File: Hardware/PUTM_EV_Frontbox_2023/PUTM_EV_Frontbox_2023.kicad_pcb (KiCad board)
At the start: 4 copper layers, 97 x 70 mm, 236 parts, among them J1 Conn_02x15_Counter_Clockwise, J3 STLINK-V3MINIE, K2 FINDER-32.21-x000, Q1 NX7002AK, SW1 Reset switch, U1 STM32G473RCTx, U10 TLP291-4, U11 TLP291-4, U12 MCP2542FDxMF, U13 MCP6001, U14 MCP6N11-005, U15 MCP6001, U16 MCP6N11-005, U17 MCP6002-xMC, U18 MCP6N11-005, U19 TLV743P, U2 MCP6002-xMC, U20 LM4040DBZ-5, U21 MCP6001, U22 MCP6N11-005, U23 MCP6001, U24 MCP6001, U25 MCP6N11-005, U26 MCP6001, U3 IMS330DHCX, U4 TLV743P, U5 TLV743P, U6 BD50FC0FP, U7 LM62440-Q1, U8 MCP2542FDxMF, U9 MCP6N11-005, Y1 ABM8G-48.000MHZ

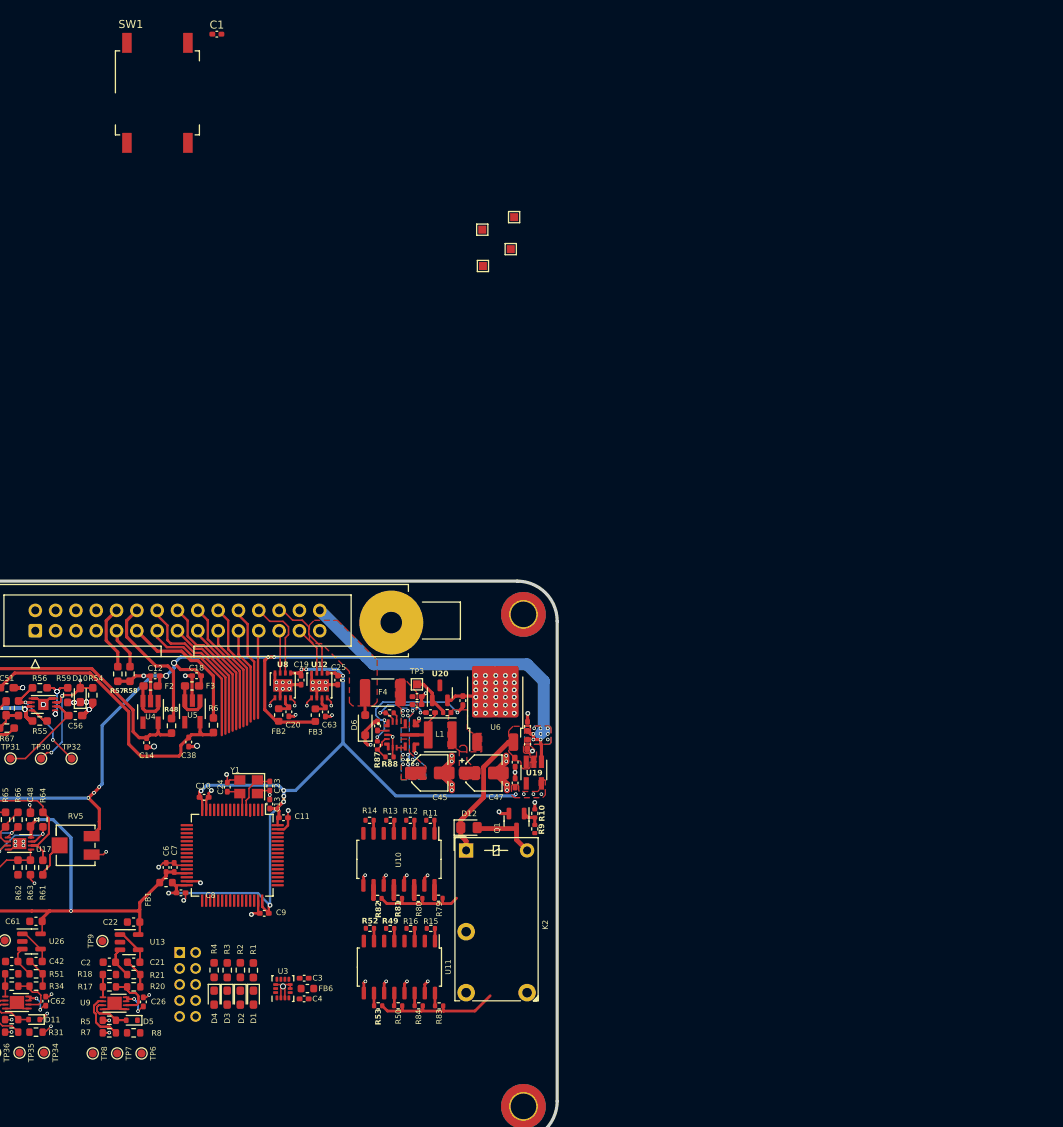
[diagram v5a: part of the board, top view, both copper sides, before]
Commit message: Changed mcu pinout
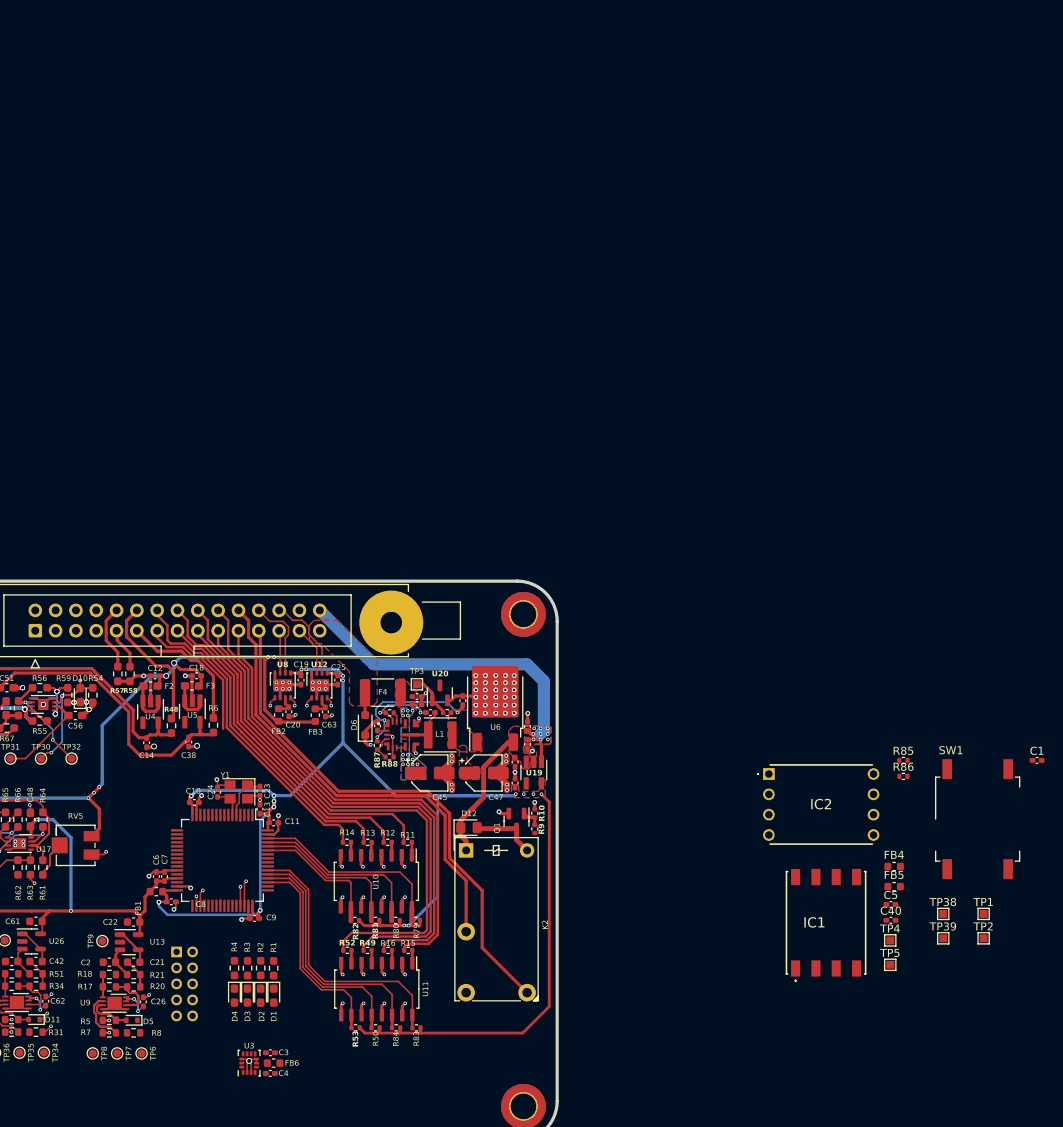
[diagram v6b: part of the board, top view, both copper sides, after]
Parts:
- added C40: 100nF, Capacitor_SMD:C_0402_1005Metric_Pad0.74x0.62mm_HandSolder, F.Cu at (243.7, 60.4)
- added C5: 100nF, Capacitor_SMD:C_0402_1005Metric_Pad0.74x0.62mm_HandSolder, F.Cu at (243.7, 58.4)
- added FB4: 60R@100MHz, Inductor_SMD:L_0603_1608Metric, F.Cu at (244.1, 53.6)
- added FB5: 60R@100MHz, Inductor_SMD:L_0603_1608Metric, F.Cu at (244.1, 56.2)
- added IC1: ELVH-MF12D-HRRJ-C-N3A4, Frontbox:ELVH005DHRRJINAA4, F.Cu at (235.6, 60.7)
- added IC2: ELVH-MF12D-HRRJ-C-N3A4, Frontbox:ELVHL10DHRRDCN2A4, F.Cu at (228.4, 42.1)
- added R85: 4k7, Resistor_SMD:R_0402_1005Metric, F.Cu at (245.2, 40.4)
- added R86: 4k7, Resistor_SMD:R_0402_1005Metric, F.Cu at (245.2, 42.4)
- added TP4: TestPoint, TestPoint:TestPoint_Pad_1.0x1.0mm, F.Cu at (243.6, 62.9)
- added TP5: TestPoint, TestPoint:TestPoint_Pad_1.0x1.0mm, F.Cu at (243.6, 65.9)
- moved SW1 136.9 mm to (254.5, 47.7)
- moved C1 136.9 mm to (262.0, 40.4)
- moved TP39 105.7 mm to (250.2, 62.6), turned to 0 degrees
- moved TP1 105.0 mm to (255.3, 59.6), turned to 0 degrees
- moved TP2 104.5 mm to (255.3, 62.6), turned to 0 degrees
- moved TP38 99.3 mm to (250.2, 59.6), turned to 0 degrees
- moved FB6 10.2 mm to (166.5, 78.2)
- moved C3 10.2 mm to (166.1, 76.9)
- moved C4 10.2 mm to (166.1, 79.5)
- moved U3 10.2 mm to (163.5, 78.2)
- moved R11 3.94 mm to (183.3, 50.6)
- moved R12 3.94 mm to (180.8, 50.6)
- moved R13 3.94 mm to (178.3, 50.6)
- moved R14 3.94 mm to (175.7, 50.6)
- moved R80 3.94 mm to (181.8, 60.4)
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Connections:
- R11 pad 1: /KILL_LEWY -> /BSPD_SENSE
- R13 pad 1: /KILL_KIERA -> /OVERTRAVEL
- R14 pad 1: /INERTIA -> /RIGHT_WHEEL_SC
- R15 pad 1: /BSPD_SENSE -> /KILL_KIERA
- R16 pad 1: /OVERTRAVEL -> /KILL_LEWY
- R52 pad 1: /Safety sense/Safety_Left_Wheel -> /INERTIA
- R53 pad 2: /Safety sense/Sens_Left_Wheel -> /Sense_inertia
- R79 pad 2: /Sense_left -> /Sense_BSPD
- R81 pad 2: /Sense_driver -> /Sense_overtravel
- R82 pad 2: /Sense_inertia -> /Sense_Right_Wheel
- R83 pad 2: /Sense_BSPD -> /Sense_driver
- R84 pad 2: /Sense_overtravel -> /Sense_left
- U1 pad 12: /Safety_control -> unconnected-(U1-PA0-Pad12)
- U1 pad 17: /APPS_sig2 -> /APPS_sig1
- U1 pad 18: /APPS_sig1 -> /APPS_sig2
- U1 pad 21: /SUSP_R_OUT -> /SUSP_L_OUT
- U1 pad 22: /SUSP_L_OUT -> /BRAKE_PRESSURE_FRONT_OUT
- U1 pad 23: /BRAKE_PRESSURE_REAR_OUT -> /SUSP_R_OUT
- U1 pad 24: /BRAKE_PRESSURE_FRONT_OUT -> /BRAKE_PRESSURE_REAR_OUT
- U1 pad 34: /CAN1_RX -> /CAN2_RX
- U1 pad 35: /CAN1_TX -> /CAN2_TX
- U1 pad 36: /DEBUG_LED4 -> unconnected-(U1-PB14-Pad36)
- U1 pad 37: /DEBUG_LED3 -> unconnected-(U1-PB15-Pad37)
- U1 pad 38: /DEBUG_LED2 -> unconnected-(U1-PC6-Pad38)
- U1 pad 39: /DEBUG_LED1 -> unconnected-(U1-PC7-Pad39)
- U1 pad 40: /YAWPROBE_I^{2}C_SCL -> unconnected-(U1-PC8-Pad40)
- U1 pad 41: /YAWPROBE_I^{2}C_SDA -> unconnected-(U1-PC9-Pad41)
- U1 pad 45: unconnected-(U1-PA11-Pad45) -> /CAN1_RX
- U1 pad 46: unconnected-(U1-PA12-Pad46) -> /CAN1_TX
- U1 pad 51: unconnected-(U1-PA15-Pad51) -> /Sense_inertia
- U1 pad 52: unconnected-(U1-PC10-Pad52) -> /Sense_EBS
- U1 pad 53: /Sense_driver -> /Sense_left
- U1 pad 54: /Sense_right -> /Sense_driver
- U1 pad 55: /Sense_inertia -> unconnected-(U1-PD2-Pad55)
- U1 pad 59: /Sense_left -> /Sense_Right_Wheel
- U1 pad 60: /Sense_EBS -> /Sense_overtravel
- U1 pad 61: /Sense_overtravel -> /Sense_right
- U10 pad 10: /Sense_inertia -> /Sense_Right_Wheel
- U10 pad 12: /Sense_driver -> /Sense_overtravel
- U10 pad 16: /Sense_left -> /Sense_BSPD
- U11 pad 10: /Safety sense/Sens_Left_Wheel -> /Sense_inertia
- U11 pad 14: /Sense_overtravel -> /Sense_left
- U11 pad 16: /Sense_BSPD -> /Sense_driver
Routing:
- net +3.3V: track 136.1 -> 192.0 mm, vias 14 -> 16
- net /SAFE-IN: track 11.0 -> 65.8 mm
- net /INERTIA: track 16.8 -> 70.3 mm
- net /EBS_SAFETY: track 13.2 -> 64.6 mm
- net /KILL_LEWY: track 15.8 -> 65.4 mm
- net /KILL_KIERA: track 12.0 -> 59.9 mm
- net /SAFE-OUT: track 14.4 -> 59.0 mm
- net /CAN2_RX: track 1.18 -> 37.0 mm, vias 1 -> 2
- net /CAN2_TX: track 1.21 -> 35.2 mm, vias 1 -> 2
- net /Sense_driver: track 1.62 -> 34.1 mm
- net /Sense_left: track 1.60 -> 31.4 mm
- net /CAN1_RX: track 1.19 -> 29.4 mm, vias 1 -> 2
- net /CAN1_TX: track 1.21 -> 29.3 mm, vias 1 -> 2
- net /BSPD_SENSE: track 14.3 -> 41.7 mm
- net /Sense_EBS: track 1.60 -> 28.6 mm
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
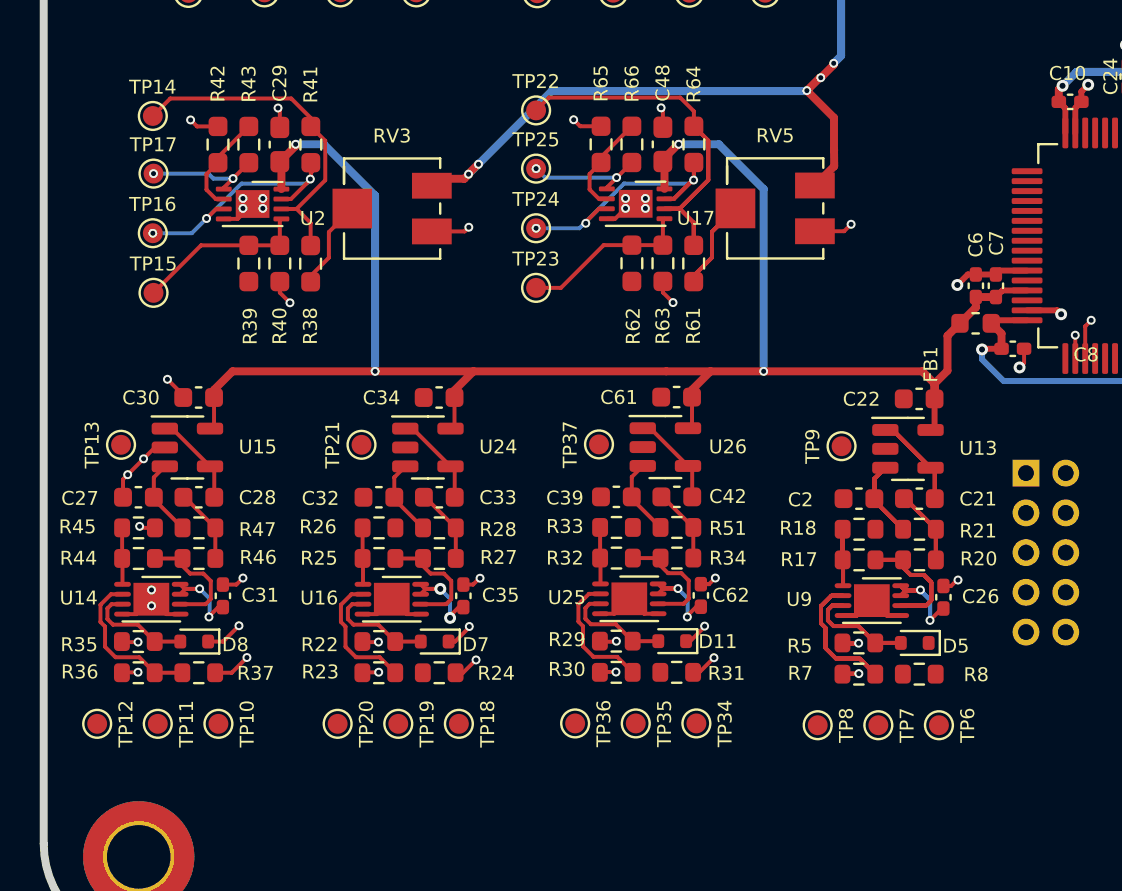
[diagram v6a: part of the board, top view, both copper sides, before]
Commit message: Changed analog section
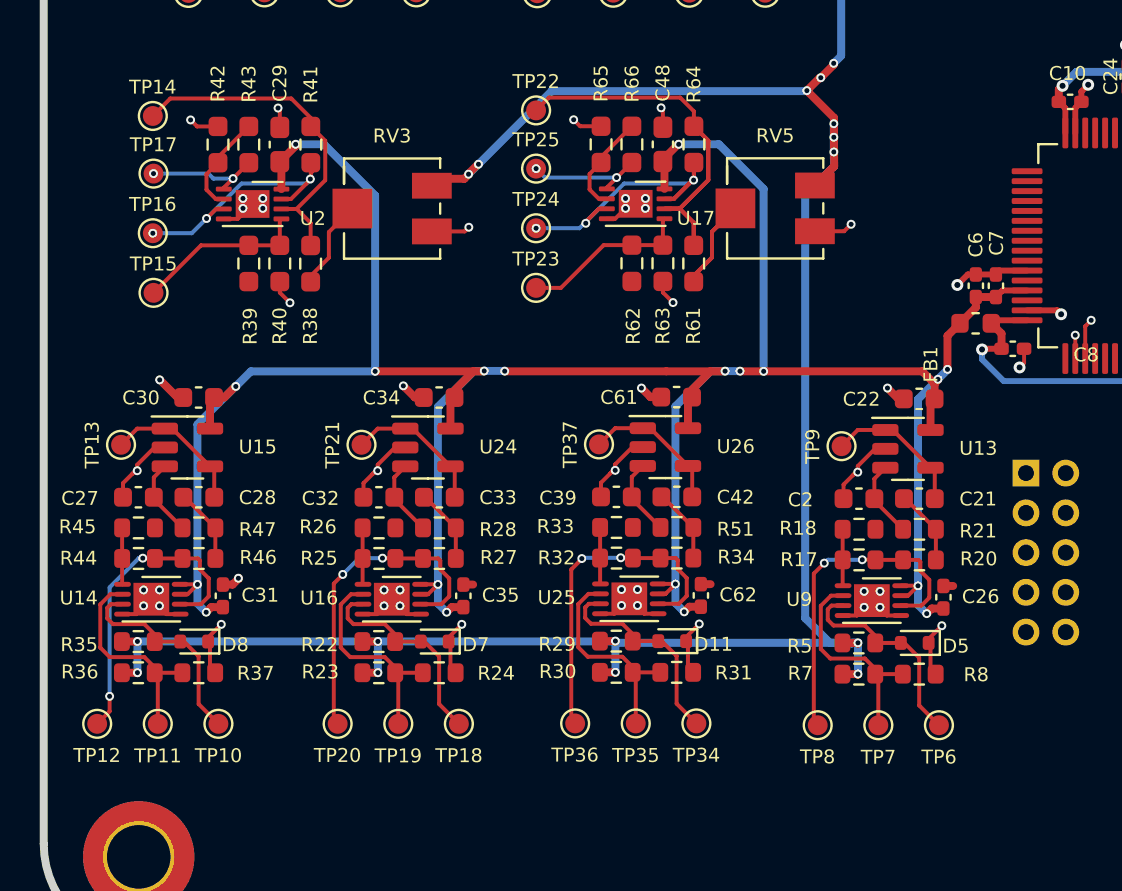
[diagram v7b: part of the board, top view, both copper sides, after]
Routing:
- net +5V: track 167.0 -> 235.4 mm, vias 26 -> 29
- net +3.3VA: track 121.3 -> 152.9 mm, vias 12 -> 19
- net Net-(R32-Pad2): track 6.06 -> 17.3 mm, vias 0 -> 2
- net Net-(R25-Pad2): track 6.06 -> 16.7 mm, vias 0 -> 2
- net Net-(R44-Pad2): track 6.06 -> 16.2 mm, vias 0 -> 2
- net GND: track 237.4 -> 247.4 mm, vias 163 -> 176
- net /Brake Position/IN+: track 19.7 -> 10.9 mm
- net Net-(U13-+): track 11.8 -> 3.92 mm
- net Net-(C21-Pad1): track 11.3 -> 3.78 mm
- net /BRAKE_POSITION_OUT: track 14.1 -> 7.25 mm
- net /BRAKE_POSITION_IN: track 16.6 -> 10.8 mm
- net Net-(U9-FG): track 8.54 -> 2.85 mm
- net /SUSPENSION_POT1_IN: track 5.52 -> 10.8 mm
- net /STEERING_POSITION_IN: track 5.52 -> 10.8 mm
- net /SUSPENSION_POT2_IN: track 5.52 -> 10.8 mm
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
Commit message: routing done
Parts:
- removed C1, C40, C5: 100nF, Capacitor_SMD:C_0402_1005Metric_Pad0.74x0.62mm_HandSolder
- removed FB4, FB5: 60R@100MHz, Inductor_SMD:L_0603_1608Metric
- removed IC1: ELVH-MF12D-HRRJ-C-N3A4, Frontbox:ELVH005DHRRJINAA4
- removed IC2: ELVH-MF12D-HRRJ-C-N3A4, Frontbox:ELVHL10DHRRDCN2A4
- removed R85, R86: 4k7, Resistor_SMD:R_0402_1005Metric
- removed SW1: Reset switch, Button_Switch_SMD:SW_MEC_5GSH9
- removed TP1, TP2, TP38, TP39, TP4, TP5: TestPoint, TestPoint:TestPoint_Pad_1.0x1.0mm
- added R68: 10k, Resistor_SMD:R_0603_1608Metric_Pad0.98x0.95mm_HandSolder, F.Cu at (167.0, 65.7)
- added R75: 10k, Resistor_SMD:R_0603_1608Metric_Pad0.98x0.95mm_HandSolder, F.Cu at (165.5, 65.7)
- moved U3 14.1 mm to (169.5, 65.5), turned to 0 degrees
- moved C4 11.5 mm to (168.2, 68.2), turned to -90 degrees
- moved FB6 10.1 mm to (169.5, 68.6), turned to 90 degrees
- moved C3 9.93 mm to (170.8, 68.2), turned to -90 degrees
- moved D1 3.89 mm to (163.5, 72.2)
- moved R1 3.89 mm to (163.4, 68.7)
- moved R3 3.89 mm to (160.2, 68.7)
- moved D2 3.89 mm to (161.8, 72.2)
- moved D3 3.89 mm to (160.2, 72.2)
- moved D4 3.89 mm to (158.6, 72.2)
- moved R2 3.89 mm to (161.8, 68.7)
- moved R4 3.89 mm to (158.6, 68.7)
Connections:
- J1 pad 3: /BRAKE_POSITION_IN -> /BRAKE_PRESSURE1_IN
- J1 pad 4: /STEERING_POSITION_IN -> /SUSPENSION_POT1_IN
- J1 pad 5: /BRAKE_PRESSURE1_IN -> /STEERING_POSITION_IN
- J1 pad 7: /SUSPENSION_POT1_IN -> /BRAKE_POSITION_IN
- J1 pad 8: /BRAKE_PRESSURE1_IN -> /BRAKE_PRESSURE2_IN
- U1 pad 17: /APPS_sig1 -> /APPS_sig2
- U1 pad 18: /APPS_sig2 -> /APPS_sig1
- U1 pad 21: /SUSP_L_OUT -> /BRAKE_PRESSURE_REAR_OUT
- U1 pad 23: /SUSP_R_OUT -> /SUSP_L_OUT
- U1 pad 24: /BRAKE_PRESSURE_REAR_OUT -> /STEERING_POSITION_OUT
- U1 pad 25: /BRAKE_POSITION_OUT -> /SUSP_R_OUT
- U1 pad 26: /STEERING_POSITION_OUT -> /BRAKE_POSITION_OUT
- U1 pad 36: unconnected-(U1-PB14-Pad36) -> /DEBUG_LED4
- U1 pad 37: unconnected-(U1-PB15-Pad37) -> /DEBUG_LED3
- U1 pad 38: unconnected-(U1-PC6-Pad38) -> /DEBUG_LED2
- U1 pad 39: unconnected-(U1-PC7-Pad39) -> /DEBUG_LED1
- U1 pad 40: unconnected-(U1-PC8-Pad40) -> /IMU_SCL
- U1 pad 41: unconnected-(U1-PC9-Pad41) -> /IMU_SDA
- U1 pad 43: unconnected-(U1-PA9-Pad43) -> /UART_TX
- U1 pad 44: unconnected-(U1-PA10-Pad44) -> /UART_RX
- U3 pad 1: /IMU_MISO -> unconnected-(U3-SDO/SA0-Pad1)
- U3 pad 12: GND -> +3.3V
- U3 pad 13: /IMU_CLK -> /IMU_SCL
- U3 pad 14: /IMU_MOSI -> /IMU_SDA
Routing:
- net /BRAKE_POSITION_IN: track 10.8 -> 99.5 mm, vias 0 -> 1
- net /SUSPENSION_POT2_IN: track 10.8 -> 92.5 mm, vias 0 -> 1
- net /SUSPENSION_POT1_IN: track 10.8 -> 91.0 mm, vias 0 -> 1
- net /STEERING_POSITION_IN: track 10.8 -> 83.9 mm, vias 0 -> 1
- net /BRAKE_PRESSURE1_IN: track 0.00 -> 52.7 mm, vias 0 -> 1
- net /BRAKE_PRESSURE_FRONT_OUT: track 5.95 -> 55.1 mm, vias 2 -> 3
- net /SUSP_L_OUT: track 7.25 -> 55.7 mm, vias 0 -> 2
- net /APPS_sig1: track 15.6 -> 61.7 mm
- net +3.3V: track 192.0 -> 237.3 mm, vias 16 -> 10
- net /DAC1_REF: track 11.7 -> 51.5 mm, vias 0 -> 2
- net /BRAKE_PRESSURE2_IN: track 0.00 -> 38.3 mm, vias 0 -> 1
- net /STEERING_POSITION_OUT: track 7.25 -> 42.2 mm, vias 0 -> 2
- net /NRST: track 0.00 -> 30.8 mm, vias 0 -> 1
- net /BRAKE_PRESSURE_REAR_OUT: track 6.09 -> 36.0 mm, vias 2 -> 3
- net /APPS_sig2: track 45.7 -> 74.0 mm
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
